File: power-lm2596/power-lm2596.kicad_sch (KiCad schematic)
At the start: 3 parts, among them J1 Screw_Terminal_01x04, J3 Conn_01x06_Female, SW1 SW_DIP_x02

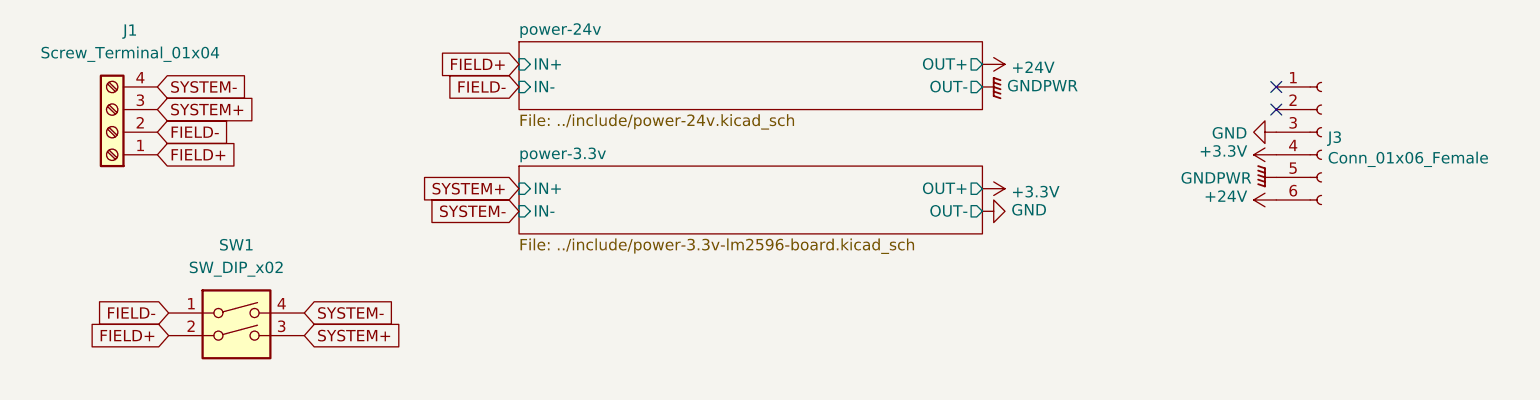
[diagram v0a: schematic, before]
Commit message: refactor power-lm2596
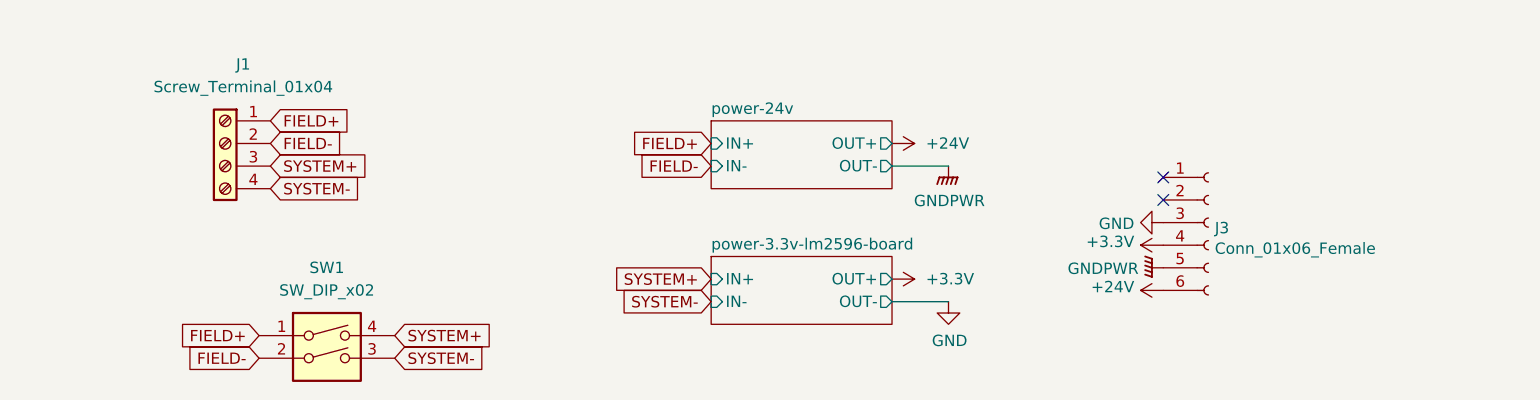
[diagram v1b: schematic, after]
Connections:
- net FIELD+: now also SW1.1; no longer SW1.2
- net FIELD-: now also SW1.2; no longer SW1.1
- net SYSTEM+: now also SW1.4; no longer SW1.3
- net SYSTEM-: now also SW1.3; no longer SW1.4
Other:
- removed sheet power-3.3v
- added sheet power-3.3v-lm2596-board (../include/power-3.3v-lm2596-board.kicad_sch)
- moved on the sheet: J3
